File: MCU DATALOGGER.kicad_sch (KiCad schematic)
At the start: 25 parts, among them U1 24LC1025, U2 24LC1025, U4 ATMEGA328P-AU, U5 DS1337S_, Y1 32.768 KHz, Y2 16 MHz

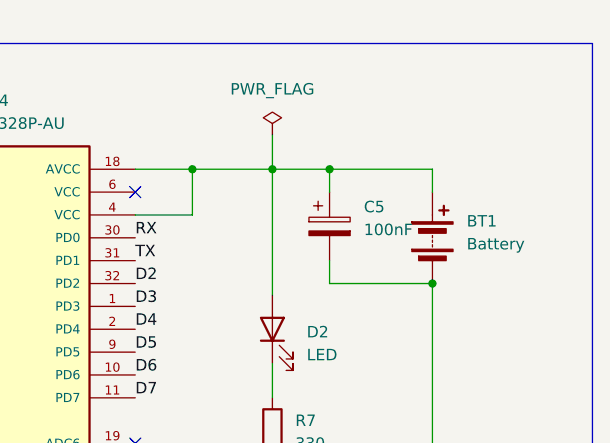
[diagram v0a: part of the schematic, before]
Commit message: Updated PCB For 2 Layer
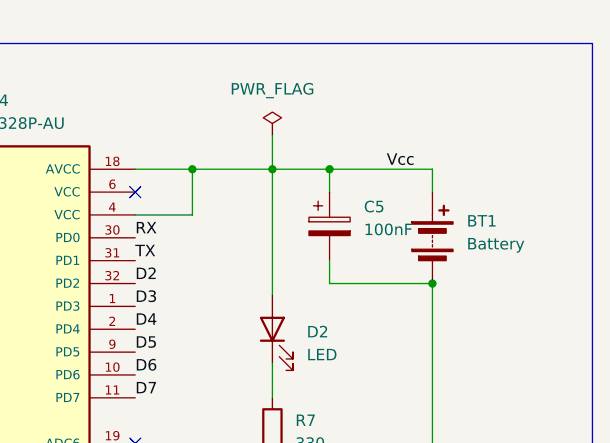
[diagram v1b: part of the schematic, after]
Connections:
- net Vcc: now also BT1.1 (+), C5.1, D2.2 (A), U4.18 (AVCC), U4.4 (VCC)
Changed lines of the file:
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@@
+		)
+	)
+	(label "Vcc"
+		(at 247.65 38.1 0)
+		(effects
+			(font
+				(size 1.27 1.27)
+			)
+			(justify left bottom)
 		)
 	)
